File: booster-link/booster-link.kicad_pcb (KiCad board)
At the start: 2 copper layers, 50 x 50 mm, 25 parts, among them P1 Conn_01x04, P2 IBT-2, P3 EXTCON, P4 CONN_01X03, Q1 BC517, Q2 BC517, U1 7805, U2 6N137

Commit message: wip
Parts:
- removed Q2: BC517, TO_SOT_Packages_THT:TO-92_Inline_Narrow_Oval
- added C11: 100nF, w_capacitors:cnp_3mm_disc, F.Cu at (130.0, 144.3)
- added C12: 2.2uF, Capacitors_ThroughHole:C_Rect_L7_W2_P5, F.Cu at (121.2, 150.4)
- added D11: 1N4148, w_pth_diodes:diode_do35, F.Cu at (124.0, 159.6)
- added D3: Led_Small, LEDs:LED-5MM, F.Cu at (135.3, 151.1)
- added Q21: BC517, TO_SOT_Packages_THT:TO-92_Inline_Narrow_Oval, F.Cu at (165.0, 129.4)
- added R11: 100k, w_pth_resistors:RC03, F.Cu at (132.5, 159.6)
- added R12: 100k, w_pth_resistors:RC03, F.Cu at (122.0, 147.1)
- added R21: 1k5, w_pth_resistors:RC03, F.Cu at (166.6, 131.3)
- added R22: 390, w_pth_resistors:RC03, F.Cu at (166.0, 126.1)
- added U11: TLC555CP, w_pth_circuits:dil_8-300_socket, F.Cu at (128.0, 153.3)
- moved R5 19.8 mm to (173.9, 118.7)
- moved D1 12.7 mm to (157.4, 116.5)
- moved R1 12.7 mm to (157.4, 113.9)
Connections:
- D2 pad 1: Net-(D2-Pad1) -> GND
- D2 pad 2: VCC -> Net-(D2-Pad2)
- Q1 pad 2: /LPWM -> Net-(Q1-Pad2)
- R2 pad 2: Net-(R2-Pad2) -> /LPWM
- R3 pad 1: /LPWM -> Net-(Q1-Pad2)
- R3 pad 2: Net-(R2-Pad2) -> /LPWM
- R5 pad 1: Net-(Q2-Pad2) -> /ENABLE
- R5 pad 2: /EN -> Net-(D3-Pad2)
- R7 pad 1: GND -> Net-(D2-Pad2)
- R7 pad 2: Net-(D2-Pad1) -> VCC
- U2 pad 1: (no net) -> Net-(U2-Pad1)
- U2 pad 4: (no net) -> Net-(U2-Pad4)
- U2 pad 6: Net-(R2-Pad2) -> /LPWM
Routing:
- net VCC: track 96.2 -> 0.80 mm
- net /LPWM: track 61.4 -> 0.00 mm, vias 1 -> 0
- net /RPWM: track 51.9 -> 0.46 mm, vias 1 -> 0
- net /SENSE: track 35.3 -> 3.34 mm
- net /EN: track 30.7 -> 0.38 mm
- net /brown: track 26.6 -> 0.00 mm
- net /18V+: track 24.0 -> 0.05 mm
- net Net-(P4-Pad1): track 21.0 -> 0.00 mm
- net /red: track 17.1 -> 0.00 mm
- net Net-(R2-Pad2): track 15.7 -> 0.00 mm
- net Net-(Q2-Pad2): track 14.8 -> 0.00 mm, vias 1 -> 0
- net Net-(D2-Pad1): track 8.94 -> 0.00 mm
- net /ENABLE: track 11.6 -> 2.84 mm
- net Net-(D1-Pad2): track 7.51 -> 0.00 mm
- net Net-(D2-Pad2): track 0.00 -> 0.63 mm

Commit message: wip
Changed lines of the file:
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@@
-(kicad_pcb (version 4) (host pcbnew 4.0.2+dfsg1-stable)
+(kicad_pcb (version 4) (host pcbnew 4.0.7-e2-6376~58~ubuntu16.04.1)
   (general
     (links 66)
     (no_connects 64)
-    (area 120.374999 93.774999 170.525001 143.925001)
+    (area 102.450001 82.65 185.025811 163.1332)
     (thickness 1.6)
     (drawings 27)
@@
   )
   (module w_pth_resistors:RC03 (layer F.Cu)
-    (at 173.863 118.745 90)
+    (at 157.353 113.919 180)
     (descr "Resistor, RC03")
     (tags R)
     (autoplace_cost180 10)
-    (fp_text reference R5 (at 0 0 90) (layer F.SilkS)
-      (effects (font (size 1 1)))
-    )
-    (fp_text value 1k5 (at 0 2 90) (layer F.SilkS) hide
-      (effects (font (size 1 1)))
+    (fp_text reference R1 (at 0 0 180) (layer F.SilkS)
+      (effects (font (size 1 1) (thickness 0.15)))
+    )
+    (fp_text value 1k5 (at 0 2 180) (layer F.SilkS) hide
+      (effects (font (size 1 1) (thickness 0.15)))
     )
     (fp_line (start 2 0) (end 3 0) (layer F.SilkS) (width 0))
@@
     (fp_line (start 2 0) (end 2 0) (layer F.SilkS) (width 0))
     (fp_line (start 2 0) (end -2 0) (layer F.SilkS) (width 0))
-    (pad 1 thru_hole circle (at -3 0 90) (size 1 1) (layers *.Cu *.Mask F.SilkS)
-      (net 7 /ENABLE))
-    (pad 2 thru_hole circle (at 3 0 90) (size 1 1) (layers *.Cu *.Mask F.SilkS)
-      (net 16 "Net-(D3-Pad2)"))
+    (pad 1 thru_hole circle (at -3 0 180) (size 1 1) (drill 0.762) (layers *.Cu *.Mask F.SilkS)
+      (net 12 "Net-(D1-Pad2)"))
+    (pad 2 thru_hole circle (at 3 0 180) (size 1 1) (drill 0.762) (layers *.Cu *.Mask F.SilkS)
+      (net 3 /red))
     (model walter/pth_resistors/rc03.wrl
       (at (xyz 0 0 0))
@@
   )
   (module w_pth_resistors:RC03 (layer F.Cu)
-    (at 157.353 113.919 180)
+    (at 173.863 118.745 90)
     (descr "Resistor, RC03")
     (tags R)
     (autoplace_cost180 10)
-    (fp_text reference R1 (at 0 0 180) (layer F.SilkS)
-      (effects (font (size 1 1)))
-    )
-    (fp_text value 1k5 (at 0 2 180) (layer F.SilkS) hide
-      (effects (font (size 1 1)))
-    )
-    (fp_line (start 2 0) (end 3 0) (layer F.SilkS) (width 0))
-    (fp_line (start -2 0) (end -3 0) (layer F.SilkS) (width 0))
-    (fp_line (start -2 0) (end -2 0) (layer F.SilkS) (width 0))
-    (fp_line (start -2 0) (end 2 0) (layer F.SilkS) (width 0))
-    (fp_line (start 2 0) (end 2 0) (layer F.SilkS) (width 0))
-    (fp_line (start 2 0) (end -2 0) (layer F.SilkS) (width 0))
-    (pad 1 thru_hole circle (at -3 0 180) (size 1 1) (layers *.Cu *.Mask F.SilkS)
-      (net 12 "Net-(D1-Pad2)"))
-    (pad 2 thru_hole circle (at 3 0 180) (size 1 1) (layers *.Cu *.Mask F.SilkS)
-      (net 3 /red))
+    (fp_text reference R5 (at 0 0 90) (layer F.SilkS)
+      (effects (font (size 1.397 1.27) (thickness 0.2032)))
+    )
+    (fp_text value 1k5 (at 0 2.032 90) (layer F.SilkS) hide
+      (effects (font (size 1.397 1.27) (thickness 0.2032)))
+    )
+    (fp_line (start 2.159 0) (end 3.81 0) (layer F.SilkS) (width 0.254))
+    (fp_line (start -2.159 0) (end -3.81 0) (layer F.SilkS) (width 0.254))
+    (fp_line (start -2.159 -0.889) (end -2.159 0.889) (layer F.SilkS) (width 0.254))
+    (fp_line (start -2.159 0.889) (end 2.159 0.889) (layer F.SilkS) (width 0.254))
+    (fp_line (start 2.159 0.889) (end 2.159 -0.889) (layer F.SilkS) (width 0.254))
+    (fp_line (start 2.159 -0.889) (end -2.159 -0.889) (layer F.SilkS) (width 0.254))
+    (pad 1 thru_hole circle (at -3.81 0 90) (size 1.99898 1.99898) (drill 0.8001) (layers *.Cu *.Mask F.SilkS)
+      (net 7 /ENABLE))
+    (pad 2 thru_hole circle (at 3.81 0 90) (size 1.99898 1.99898) (drill 0.8001) (layers *.Cu *.Mask F.SilkS)
+      (net 16 "Net-(D3-Pad2)"))
     (model walter/pth_resistors/rc03.wrl
       (at (xyz 0 0 0))

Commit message: add Gerber files
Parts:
- G***: footprint w_logo:Logo_copper_CC-BY-NC-SA_5x2mm -> w_logo:Logo_copper_CC-BY-NC-SA_10x3.6mm
- moved D11 47.8 mm to (139.7, 114.6), turned to 0 degrees
- moved U11 34.1 mm to (139.4, 121.2)
- moved R5 34.1 mm to (143.6, 134.5), turned to 270 degrees
- moved R11 32.6 mm to (139.4, 127.8)
- moved G*** 31.0 mm to (135.4, 106.6)
- moved R12 31.0 mm to (133.1, 118.1), turned to 90 degrees
- moved C11 30.3 mm to (146.2, 118.6), turned to 270 degrees
- moved C12 25.9 mm to (133.1, 127.4)
- moved R21 22.1 mm to (166.6, 109.2), turned to 90 degrees
- moved R22 17.0 mm to (164.1, 109.2), turned to 270 degrees
- moved R4 15.1 mm to (153.2, 135.3), turned to 180 degrees
- moved D3 14.9 mm to (135.9, 136.3)
- moved R7 14.2 mm to (135.4, 142.5), turned to 0 degrees
- moved R3 13.8 mm to (146.2, 134.5), turned to 90 degrees
- moved Q21 12.6 mm to (164.3, 116.8)
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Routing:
- net VCC: track 0.80 -> 113.8 mm
- net /LPWM: track 0.00 -> 70.4 mm, vias 0 -> 1
- net /EN: track 0.38 -> 63.2 mm
- net /RPWM: track 0.46 -> 43.8 mm
- net Net-(P4-Pad1): track 0.00 -> 38.1 mm, vias 0 -> 1
- net /ENABLE: track 2.84 -> 32.1 mm
- net /18V+: track 0.05 -> 25.1 mm
- net /SENSE: track 3.34 -> 26.7 mm
- net Net-(C12-Pad1): track 0.00 -> 20.5 mm
- net /brown: track 0.00 -> 18.2 mm
- net /red: track 0.00 -> 8.95 mm
- net Net-(D1-Pad2): track 0.00 -> 6.70 mm
- net Net-(D3-Pad2): track 0.00 -> 6.45 mm
- net Net-(D2-Pad2): track 0.63 -> 6.22 mm
- net Net-(Q21-Pad2): track 0.00 -> 4.23 mm
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
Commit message: wip
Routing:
- net GND: track 0.00 -> 31.6 mm, vias 0 -> 9
- net /EN: track 63.2 -> 64.9 mm
- net VCC: track 113.8 -> 115.1 mm
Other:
- board text added: "GND VCC LPWM EN RPWM SEN"
- board text removed: "GND VCC LPWM EN RPWM SENSE"
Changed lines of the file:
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@@
     (thickness 1.6)
     (drawings 28)
-    (tracks 170)
+    (tracks 203)
     (zones 0)
     (modules 34)
@@
     (descr "Small ceramic capacitor")
     (tags C)
-    (fp_text reference C11 (at 2.794 2.54 360) (layer F.SilkS)
+    (fp_text reference C11 (at 3.683 0 360) (layer F.SilkS)
       (effects (font (size 1.016 1.016) (thickness 0.2032)))
     )
@@
       (xy 4.15036 -0.50546)) (layer F.Cu) (width 0.00254))
   )
-  (gr_text " GND   VCC\n\nLPWM  EN\n\nRPWM SENSE" (at 161.29 123.444) (layer F.SilkS)
-    (effects (font (size 0.8 0.6) (thickness 0.15)))
+  (gr_text " GND   VCC\n\nLPWM  EN\n\nRPWM SEN" (at 161.29 123.444) (layer F.SilkS)
+    (effects (font (size 0.89 0.7) (thickness 0.15)))
   )
   (gr_text Enable (at 137.414 140.208) (layer F.SilkS)
@@
     (arrow2b (pts (xy 108.95 93.35) (xy 109.536421 94.476504)))
   )
+  (segment (start 160.655 135.636) (end 161.417 135.636) (width 0.6) (layer B.Cu) (net 1))
+  (segment (start 160.02 132.334) (end 158.496 133.858) (width 0.6) (layer F.Cu) (net 1))
+  (via (at 158.496 133.858) (size 0.8) (drill 0.7) (layers F.Cu B.Cu) (net 1))
+  (segment (start 158.496 133.858) (end 160.274 135.636) (width 0.6) (layer B.Cu) (net 1))
+  (segment (start 160.274 135.636) (end 160.655 135.636) (width 0.6) (layer B.Cu) (net 1))
+  (segment (start 160.02 131.064) (end 160.02 132.334) (width 0.6) (layer F.Cu) (net 1))
+  (via (at 160.655 135.636) (size 0.8) (drill 0.7) (layers F.Cu B.Cu) (net 1))
+  (via (at 161.925 137.922) (size 0.8) (drill 0.7) (layers F.Cu B.Cu) (net 1))
+  (segment (start 161.925 136.144) (end 161.925 137.922) (width 0.6) (layer B.Cu) (net 1))
+  (segment (start 161.417 135.636) (end 161.925 136.144) (width 0.6) (layer B.Cu) (net 1))
+  (segment (start 146.177 141.605) (end 147.193 141.605) (width 0.6) (layer B.Cu) (net 1))
+  (via (at 150.495 137.16) (size 0.8) (drill 0.7) (layers F.Cu B.Cu) (net 1))
+  (segment (start 148.336 137.16) (end 150.495 137.16) (width 0.6) (layer F.Cu) (net 1))
+  (segment (start 148.209 137.287) (end 148.336 137.16) (width 0.6) (layer F.Cu) (net 1))
+  (via (at 148.209 137.287) (size 0.8) (drill 0.7) (layers F.Cu B.Cu) (net 1))
+  (segment (start 148.209 140.589) (end 148.209 137.287) (width 0.6) (layer B.Cu) (net 1))
+  (segment (start 147.193 141.605) (end 148.209 140.589) (width 0.6) (layer B.Cu) (net 1))
+  (via (at 167.64 129.54) (size 0.8) (drill 0.7) (layers F.Cu B.Cu) (net 1))
+  (segment (start 167.64 129.54) (end 166.116 131.064) (width 0.6) (layer B.Cu) (net 1))
+  (segment (start 166.116 131.064) (end 164.719 131.064) (width 0.6) (layer B.Cu) (net 1))
+  (segment (start 160.02 131.064) (end 164.719 131.064) (width 0.6) (layer B.Cu) (net 1))
+  (via (at 169.672 132.588) (size 0.8) (drill 0.7) (layers F.Cu B.Cu) (net 1))
+  (segment (start 166.116 132.588) (end 169.672 132.588) (width 0.6) (layer B.Cu) (net 1))
+  (segment (start 165.989 132.461) (end 166.116 132.588) (width 0.6) (layer B.Cu) (net 1))
+  (via (at 165.989 132.461) (size 0.8) (drill 0.7) (layers F.Cu B.Cu) (net 1))
+  (segment (start 165.989 132.334) (end 165.989 132.461) (width 0.6) (layer F.Cu) (net 1))
+  (segment (start 164.719 131.064) (end 165.989 132.334) (width 0.6) (layer F.Cu) (net 1))
+  (via (at 164.719 131.064) (size 0.8) (drill 0.7) (layers F.Cu B.Cu) (net 1))
+  (segment (start 123.698 111.76) (end 123.698 113.538) (width 0.6) (layer F.Cu) (net 2))
+  (segment (start 124.46 114.3) (end 133.096 114.3) (width 0.6) (layer F.Cu) (net 2))
+  (segment (start 123.698 113.538) (end 124.46 114.3) (width 0.6) (layer F.Cu) (net 2))
   (segment (start 151.43 139.45) (end 148.332 139.45) (width 0.6) (layer F.Cu) (net 2))
   (segment (start 141.605 140.081) (end 139.192 142.494) (width 0.6) (layer F.Cu) (net 2))
@@
   (segment (start 143.256 124.968) (end 135.636 117.348) (width 0.6) (layer F.Cu) (net 2))
   (segment (start 133.096 114.3) (end 133.096 115.951) (width 0.6) (layer F.Cu) (net 2))
+  (segment (start 134.493 117.348) (end 135.636 117.348) (width 0.6) (layer F.Cu) (net 2))
   (segment (start 133.096 115.951) (end 134.493 117.348) (width 0.6) (layer F.Cu) (net 2))
-  (segment (start 134.493 117.348) (end 135.636 117.348) (width 0.6) (layer F.Cu) (net 2))
   (segment (start 123.698 111.76) (end 123.698 112.395) (width 0.6) (layer F.Cu) (net 2))
-  (segment (start 123.698 112.395) (end 125.603 114.3) (width 0.6) (layer F.Cu) (net 2))
-  (segment (start 125.603 114.3) (end 133.096 114.3) (width 0.6) (layer F.Cu) (net 2))
   (segment (start 143.256 124.968) (end 143.256 127.762) (width 0.6) (layer F.Cu) (net 2))
   (segment (start 154.432 127.762) (end 154.432 127.254) (width 0.6) (layer F.Cu) (net 2))
@@
   (segment (start 146.939 111.76) (end 148.41 110.289) (width 0.6) (layer F.Cu) (net 9))
   (segment (start 128.778 111.76) (end 128.778 108.712) (width 0.6) (layer F.Cu) (net 9))
+  (segment (start 156.21 122.174) (end 155.702 122.174) (width 0.3048) (layer B.Cu) (net 10))
+  (segment (start 140.716 123.317) (end 141.605 122.428) (width 0.3048) (layer B.Cu) (net 10))
+  (segment (start 166.497 122.174) (end 160.274 122.174) (width 0.3048) (layer B.Cu) (net 10))
+  (segment (start 166.497 122.174) (end 167.767 123.444) (width 0.3048) (layer B.Cu) (net 10))
+  (segment (start 160.274 122.174) (end 156.21 122.174) (width 0.3048) (layer B.Cu) (net 10))
+  (segment (start 155.448 122.428) (end 141.605 122.428) (width 0.3048) (layer B.Cu) (net 10))
+  (segment (start 155.702 122.174) (end 155.448 122.428) (width 0.3048) (layer B.Cu) (net 10))
+  (segment (start 140.716 123.317) (end 140.716 124.968) (width 0.3048) (layer B.Cu) (net 10))
   (segment (start 168.148 123.444) (end 169.672 124.968) (width 0.3048) (layer F.Cu) (net 10))
   (segment (start 168.275 132.334) (end 168.275 134.493) (width 0.3048) (layer F.Cu) (net 10))
   (segment (start 169.672 130.937) (end 168.275 132.334) (width 0.3048) (layer F.Cu) (net 10))
   (segment (start 169.672 124.968) (end 169.672 130.937) (width 0.3048) (layer F.Cu) (net 10))
-  (segment (start 160.274 122.174) (end 141.859 122.174) (width 0.3048) (layer B.Cu) (net 10))
-  (segment (start 166.497 122.174) (end 160.274 122.174) (width 0.3048) (layer B.Cu) (net 10))
-  (segment (start 167.767 123.444) (end 166.497 122.174) (width 0.3048) (layer B.Cu) (net 10))
   (segment (start 140.716 123.317) (end 140.716 124.968) (width 0.3048) (layer B.Cu) (net 10))
-  (segment (start 141.859 122.174) (end 140.716 123.317) (width 0.3048) (layer B.Cu) (net 10))
   (segment (start 168.148 123.444) (end 167.767 123.444) (width 0.3048) (layer B.Cu) (net 10))
   (segment (start 168.148 123.444) (end 168.148 123.698) (width 0.3048) (layer F.Cu) (net 10))

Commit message: prepare next version
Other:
- board text added: "V1.01 072018 Gerhard Bertelsmann"
- board text removed: "V1.0 072018 Gerhard Bertelsmann"
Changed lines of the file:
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@@
   (title_block
     (title Booster-Link)
-    (date 2018-07-23)
+    (date 2018-07-24)
   )
   (layers
@@
     (effects (font (size 1 1) (thickness 0.2)))
   )
-  (gr_text "  V1.0 072018\nGerhard Bertelsmann" (at 135.255 109.728) (layer F.Cu)
+  (gr_text "  V1.01 072018\nGerhard Bertelsmann" (at 135.255 109.728) (layer F.Cu)
     (effects (font (size 0.6 0.6) (thickness 0.125)))
   )

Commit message: wip
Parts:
- moved P3 2.05 mm to (163.6, 120.7)
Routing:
- net VCC: track 115.1 -> 120.9 mm
- net /SENSE: track 26.7 -> 22.3 mm, vias 0 -> 1
- net /EN: track 64.9 -> 61.4 mm
- net /LPWM: track 70.4 -> 68.0 mm
- net GND: track 31.6 -> 30.1 mm
- net /RPWM: track 43.8 -> 44.7 mm
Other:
- board text added: "EN"
- board text added: "LPWM"
- board text added: "RPWM"
- board text added: "SEN"
- board text added: "VCC"
- board text removed: "GND VCC LPWM EN RPWM SEN"

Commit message: BC517 -> BC337 taht works / add pictures
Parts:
- Q1, Q21: value BC517 -> BC337
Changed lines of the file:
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@@
     (links 66)
     (no_connects 0)
-    (area 102.450001 82.65 171.985715 145.9452)
+    (area 120.374999 93.774999 170.525001 143.925001)
     (thickness 1.6)
     (drawings 33)
@@
       (effects (font (size 1 1) (thickness 0.15)))
     )
-    (fp_text value BC517 (at 1.27 -0.254) (layer F.Fab)
+    (fp_text value BC337 (at 1.27 -0.254) (layer F.Fab)
       (effects (font (size 1 1) (thickness 0.15)))
     )
@@
       (effects (font (size 1 1) (thickness 0.15)))
     )
-    (fp_text value BC517 (at 1.27 0) (layer F.Fab)
-      (effects (font (size 1 1) (thickness 0.15)))
-    )
+    (fp_text value BC337 (at 1.27 0) (layer F.Fab)
+      (effects (font (size 1 1) (thickness 0.15)))
+    )

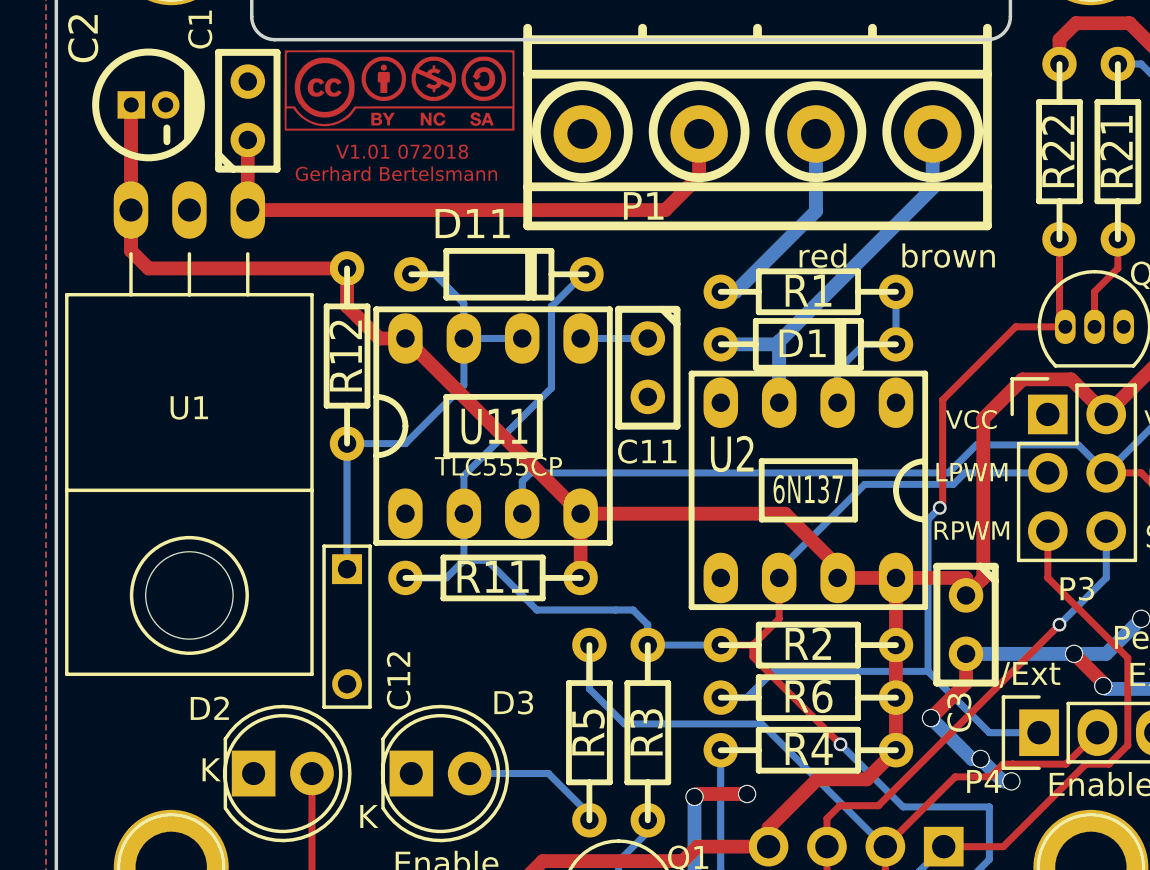
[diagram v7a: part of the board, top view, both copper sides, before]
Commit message: add some place for cap
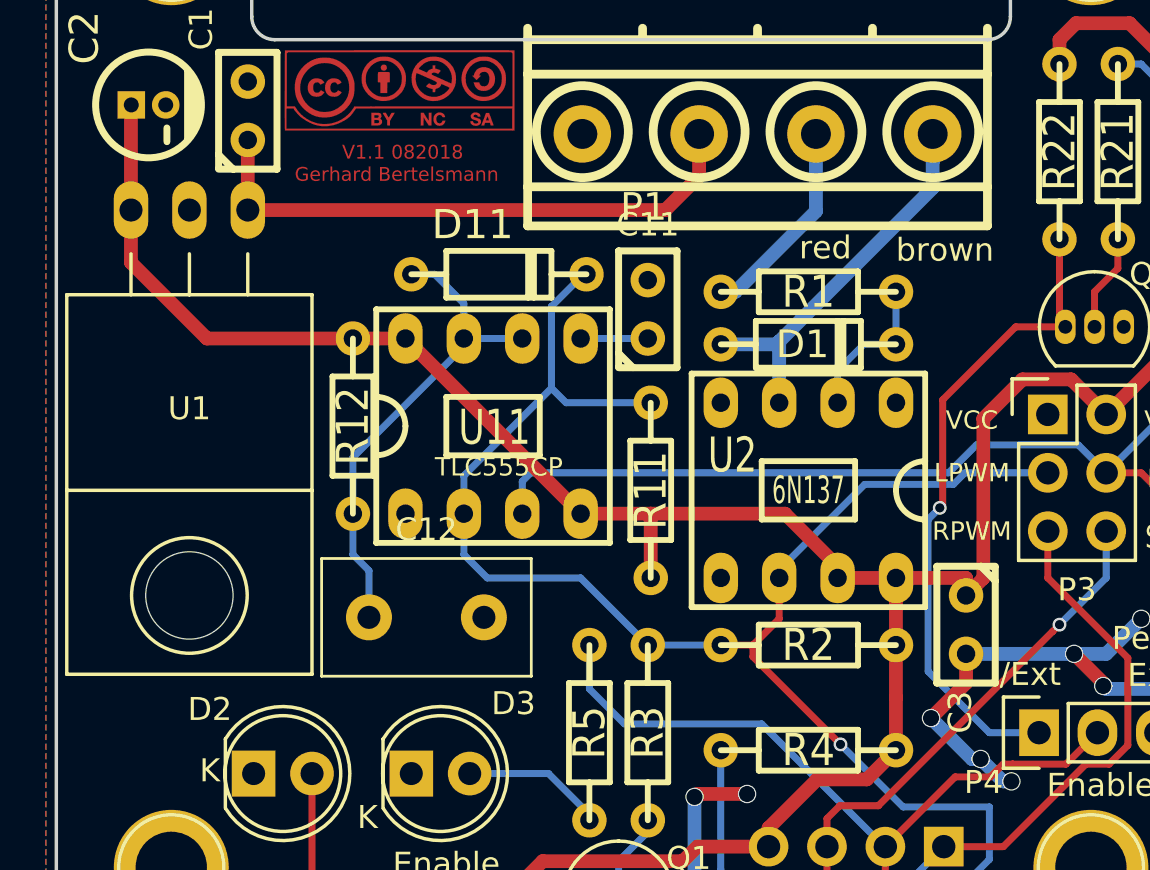
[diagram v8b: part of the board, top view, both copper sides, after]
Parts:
- removed R6: 390, w_pth_resistors:RC03
- C12: footprint Capacitors_ThroughHole:C_Rect_L7_W2_P5 -> Capacitors_THT:C_Disc_D9.0mm_W5.0mm_P5.00mm
- moved R11 7.85 mm to (146.3, 124.0), turned to 90 degrees
- moved R12 3.06 mm to (133.3, 121.2)
- moved C11 2.54 mm to (146.2, 116.1), turned to 90 degrees
- moved C12 2.30 mm to (134.0, 129.5), turned to 0 degrees
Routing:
- net Net-(P4-Pad1): track 38.1 -> 28.6 mm
- net /LPWM: track 68.0 -> 69.0 mm
- net Net-(C12-Pad1): track 20.5 -> 21.3 mm
- net VCC: track 120.9 -> 120.2 mm
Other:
- board text added: "V1.1 082018 Gerhard Bertelsmann"
- board text removed: "V1.01 072018 Gerhard Bertelsmann"
